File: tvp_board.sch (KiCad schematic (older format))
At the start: 87 parts, among them J1 VGA, J2 3XRCA_CONN, J3 SCART-F, J5 5VDC_IN, J6 SJ1-3533NG, J7 SJ1-3533NG, SW1 SPST, SW4 DPDT, U1 TVP7002PZP, U17 THS7353, U4 SN74LVC2G17, U5 AP7361C, U6 TLV70033, U7 NCP703SN19T1G, U9 TLV70019, Y1 ACHL-27MHZ-EK

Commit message: finalize pcb v1.6
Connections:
- wire segments 239 -> 237
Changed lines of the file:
@@
 EESchema Schematic File Version 2
-LIBS:ossc_board-rescue
 LIBS:power
 LIBS:device
@@
 Sheet 3 4
 Title "Open Source Scan Converter"
-Date "2017-03-12"
+Date "2017-04-14"
 Rev "1.6"
 Comp ""
@@
 	1    0    0    -1
 $EndComp
-Text Label 2250 5450 0    60   ~ 0
+Text Label 2250 5650 0    60   ~ 0
 AV1_AUD_L
-Text Label 2250 5800 0    60   ~ 0
+Text Label 2250 6000 0    60   ~ 0
 AV1_AUD_R
 $Comp
@@
 Wire Wire Line
 	9350 3450 9900 3450
-Text HLabel 2700 5650 0    60   Output ~ 0
+Text HLabel 2750 5450 0    60   Output ~ 0
 AV2_AUD_L
-Text HLabel 2700 6000 0    60   Output ~ 0
+Text HLabel 2750 5800 0    60   Output ~ 0
 AV2_AUD_R
 $Comp
@@
 L DPDT SW4
 U 1 1 58D31ED2
-P 3250 5700
-F 0 "SW4" H 3250 6100 50  0000 C CNN
-F 1 "DPDT" H 3250 5350 50  0000 C CNN
-F 2 "custom_components:MS22" H 3250 5900 50  0001 C CNN
-F 3 "" H 3250 5900 50  0000 C CNN
-	1    3250 5700
-	-1   0    0    1
-$EndComp
-Wire Wire Line
-	2250 5450 2750 5450
-Wire Wire Line
-	2750 5650 2700 5650
-Wire Wire Line
-	2250 5800 2750 5800
-Wire Wire Line
-	2700 6000 2750 6000
+P 3250 5750
+F 0 "SW4" H 3250 6150 50  0000 C CNN
+F 1 "DPDT" H 3250 5400 50  0000 C CNN
+F 2 "custom_components:MS22" H 3250 5950 50  0001 C CNN
+F 3 "" H 3250 5950 50  0000 C CNN
+	1    3250 5750
+	-1   0    0    -1
+$EndComp
+Wire Wire Line
+	2250 5650 2750 5650
+Wire Wire Line
+	2250 6000 2750 6000
 Wire Wire Line
 	3950 5800 3850 5800

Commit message: v1.6-jp21
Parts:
- J3: value SCART-F -> JP21
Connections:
- wire segments 237 -> 230
- no-connect marks 22 -> 21
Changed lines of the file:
@@
 P 1500 3550
 F 0 "J3" H 1500 4750 60  0000 C CNN
-F 1 "SCART-F" H 1540 2350 60  0000 C CNN
+F 1 "JP21" H 1540 2350 60  0000 C CNN
 F 2 "custom_components:SCART_CONN" H 1500 3550 60  0001 C CNN
 F 3 "" H 1500 3550 60  0000 C CNN
@@
 Text Label 600  5550 0    60   ~ 0
 GND
-Text Label 600  2600 0    60   ~ 0
-GND
-Text Label 600  3000 0    60   ~ 0
-GND
-Text Label 600  3400 0    60   ~ 0
-GND
-Text Label 600  3800 0    60   ~ 0
-GND
-Text Label 600  4200 0    60   ~ 0
-GND
 Text Label 550  3200 0    60   ~ 0
 RGB1_R
-Text Label 550  3600 0    60   ~ 0
+Text Label 550  2800 0    60   ~ 0
 RGB1_G
-Text Label 550  4000 0    60   ~ 0
+Text Label 2200 2650 1    60   ~ 0
 RGB1_B
-NoConn ~ 2100 3100
-NoConn ~ 900  2800
-NoConn ~ 900  4400
-NoConn ~ 900  4600
-NoConn ~ 2100 3900
-NoConn ~ 2100 3700
-NoConn ~ 2100 3500
 Text Label 600  1750 0    60   ~ 0
 RGB3_R
@@
 Text Label 9450 2750 0    60   ~ 0
 RESET_N
-Text Label 2200 2650 1    60   ~ 0
+Text Label 550  3800 0    60   ~ 0
 RGB1_S
 $Comp
@@
 	0    1    1    0
 $EndComp
-$Comp
-L GND-RESCUE-ossc_board #PWR0151
-U 1 1 55F23807
-P 2100 3300
-F 0 "#PWR0151" H 2100 3300 30  0001 C CNN
-F 1 "GND" H 2100 3230 30  0001 C CNN
-F 2 "" H 2100 3300 60  0001 C CNN
-F 3 "" H 2100 3300 60  0000 C CNN
-	1    2100 3300
-	0    -1   -1   0
-$EndComp
-$Comp
-L GND-RESCUE-ossc_board #PWR0152
-U 1 1 55F239ED
-P 2100 2900
-F 0 "#PWR0152" H 2100 2900 30  0001 C CNN
-F 1 "GND" H 2100 2830 30  0001 C CNN
-F 2 "" H 2100 2900 60  0001 C CNN
-F 3 "" H 2100 2900 60  0000 C CNN
-	1    2100 2900
-	0    -1   -1   0
-$EndComp
 Text Label 2450 2250 1    60   ~ 0
 AVDD
@@
 	0    1    1    0
 $EndComp
-$Comp
-L GND-RESCUE-ossc_board #PWR0157
-U 1 1 55F7E41D
-P 2100 4300
-F 0 "#PWR0157" H 2100 4300 30  0001 C CNN
-F 1 "GND" H 2100 4230 30  0001 C CNN
-F 2 "" H 2100 4300 60  0001 C CNN
-F 3 "" H 2100 4300 60  0000 C CNN
-	1    2100 4300
-	0    -1   -1   0
-$EndComp
-Text Label 2300 4900 1    60   ~ 0
+Text Label 500  4600 0    60   ~ 0
 AV1_AUD_L
-Text Label 2150 4900 1    60   ~ 0
+Text Label 500  4200 0    60   ~ 0
 AV1_AUD_R
 $Comp
@@
 	4400 6700 4400 6650
 Wire Wire Line
-	2150 4500 2150 4900
-Wire Wire Line
-	2100 4500 2150 4500
-Wire Wire Line
-	2300 4100 2300 4900
-Wire Wire Line
-	2100 4100 2300 4100
-Wire Wire Line
 	2450 2000 2450 2300
 Connection ~ 6200 1600
@@
 	600  1750 900  1750
 Wire Wire Line
-	900  4000 550  4000
-Wire Wire Line
-	900  3600 550  3600
+	900  3800 550  3800
+Wire Wire Line
+	900  2800 550  2800
 Wire Wire Line
 	900  3200 550  3200
-Wire Wire Line
-	900  2600 550  2600
-Wire Wire Line
-	900  3000 550  3000
-Wire Wire Line
-	900  3400 550  3400
-Wire Wire Line
-	900  3800 550  3800
-Wire Wire Line
-	900  4200 550  4200
 Wire Wire Line
 	550  5250 850  5250
@@
 Wire Wire Line
 	3950 5900 3750 5900
+Wire Wire Line
+	900  4200 500  4200
+Wire Wire Line
+	900  4600 500  4600
+$Comp
+L GND #PWR?
+U 1 1 58F0DD5B
+P 900 2600
+F 0 "#PWR?" H 900 2350 50  0001 C CNN
+F 1 "GND" H 900 2450 50  0001 C CNN
+F 2 "" H 900 2600 50  0000 C CNN
+F 3 "" H 900 2600 50  0000 C CNN
+	1    900  2600
+	0    1    1    0
+$EndComp
+$Comp
+L GND #PWR?
+U 1 1 58F0DF83
+P 900 3400
+F 0 "#PWR?" H 900 3150 50  0001 C CNN
+F 1 "GND" H 900 3250 50  0001 C CNN
+F 2 "" H 900 3400 50  0000 C CNN
+F 3 "" H 900 3400 50  0000 C CNN
+	1    900  3400
+	0    1    1    0
+$EndComp
+$Comp
+L GND #PWR?
+U 1 1 58F0E093
+P 900 3000
+F 0 "#PWR?" H 900 2750 50  0001 C CNN
+F 1 "GND" H 900 2850 50  0001 C CNN
+F 2 "" H 900 3000 50  0000 C CNN
+F 3 "" H 900 3000 50  0000 C CNN
+	1    900  3000
+	0    1    1    0
+$EndComp
+$Comp
+L GND #PWR?
+U 1 1 58F0E1A3
+P 900 4000
+F 0 "#PWR?" H 900 3750 50  0001 C CNN
+F 1 "GND" H 900 3850 50  0001 C CNN
+F 2 "" H 900 4000 50  0000 C CNN
+F 3 "" H 900 4000 50  0000 C CNN
+	1    900  4000
+	0    1    1    0
+$EndComp
+$Comp
+L GND #PWR?
+U 1 1 58F0E2B3
+P 2100 2900
+F 0 "#PWR?" H 2100 2650 50  0001 C CNN
+F 1 "GND" H 2100 2750 50  0001 C CNN
+F 2 "" H 2100 2900 50  0000 C CNN
+F 3 "" H 2100 2900 50  0000 C CNN
+	1    2100 2900
+	0    -1   -1   0
+$EndComp
+$Comp
+L GND #PWR?
+U 1 1 58F0E3C3
+P 900 4400
+F 0 "#PWR?" H 900 4150 50  0001 C CNN
+F 1 "GND" H 900 4250 50  0001 C CNN
+F 2 "" H 900 4400 50  0000 C CNN
+F 3 "" H 900 4400 50  0000 C CNN
+	1    900  4400
+	0    1    1    0
+$EndComp
+NoConn ~ 2100 4500
+NoConn ~ 2100 4100
+NoConn ~ 900  3600
+NoConn ~ 2100 3500
+NoConn ~ 2100 3700
+NoConn ~ 2100 3100
+$Comp
+L GND #PWR?
+U 1 1 58F0EABE
+P 2100 4300
+F 0 "#PWR?" H 2100 4050 50  0001 C CNN
+F 1 "GND" H 2100 4150 50  0001 C CNN
+F 2 "" H 2100 4300 50  0000 C CNN
+F 3 "" H 2100 4300 50  0000 C CNN
+	1    2100 4300
+	0    -1   -1   0
+$EndComp
+$Comp
+L GND #PWR?
+U 1 1 58F0EBCE
+P 2100 3900
+F 0 "#PWR?" H 2100 3650 50  0001 C CNN
+F 1 "GND" H 2100 3750 50  0001 C CNN
+F 2 "" H 2100 3900 50  0000 C CNN
+F 3 "" H 2100 3900 50  0000 C CNN
+	1    2100 3900
+	0    -1   -1   0
+$EndComp
+$Comp
+L GND #PWR?
+U 1 1 58F0ECDE
+P 2100 3300
+F 0 "#PWR?" H 2100 3050 50  0001 C CNN
+F 1 "GND" H 2100 3150 50  0001 C CNN
+F 2 "" H 2100 3300 50  0000 C CNN
+F 3 "" H 2100 3300 50  0000 C CNN
+	1    2100 3300
+	0    -1   -1   0
+$EndComp
 $EndSCHEMATC

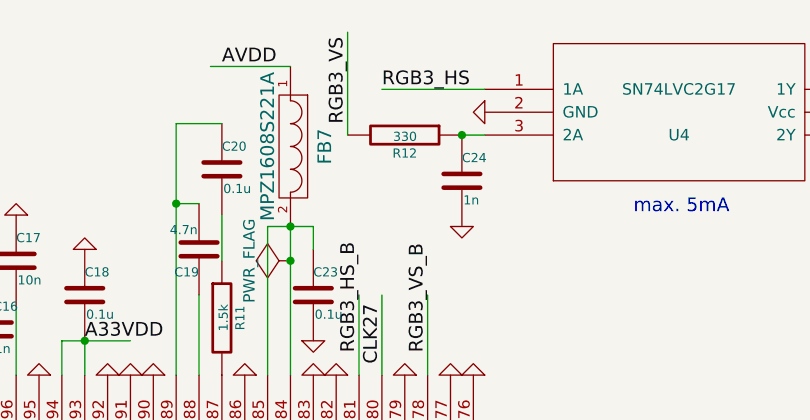
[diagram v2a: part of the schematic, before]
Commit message: Regenerate PCB files after recent small updates.
- update R12 value on schematic, netlist and layout.
- update ECS-3X9X footprint.
- add pdf of the schematic.
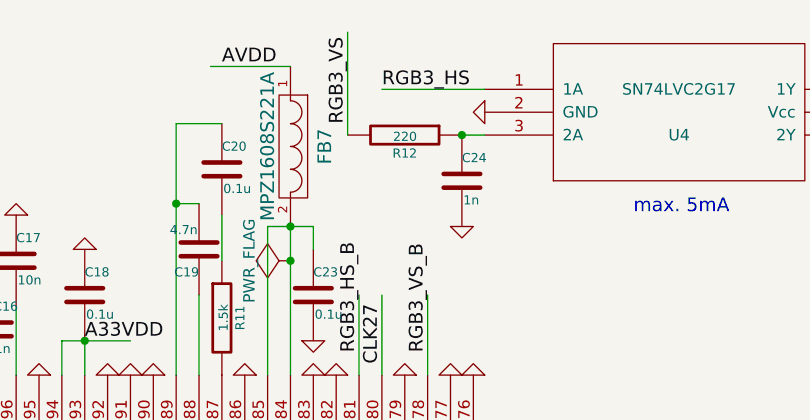
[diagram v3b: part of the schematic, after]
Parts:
- R12: value 330 -> 220
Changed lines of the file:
@@
 Sheet 3 4
 Title "Open Source Scan Converter"
-Date "2017-04-14"
-Rev "1.6"
+Date "2017-07-03"
+Rev "1.6-jp21"
 Comp ""
 Comment1 ""
@@
 P 6700 1050
 F 0 "R12" V 6780 1050 40  0000 C CNN
-F 1 "330" V 6707 1051 40  0000 C CNN
+F 1 "220" V 6707 1051 40  0000 C CNN
 F 2 "custom_components:SM0603_Resistor_libcms" V 6630 1050 30  0001 C CNN
 F 3 "~" H 6700 1050 30  0000 C CNN
